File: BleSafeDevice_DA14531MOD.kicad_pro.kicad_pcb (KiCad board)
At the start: 2 copper layers, 43.5 x 33.5 mm, 19 parts, among them J1 SWD_DEBUG_PADS, J2 CURRENT_MEAS_PADS, SW1 PTS526SK15SMTR2 LFS, U4 DA14531MOD-00F01002

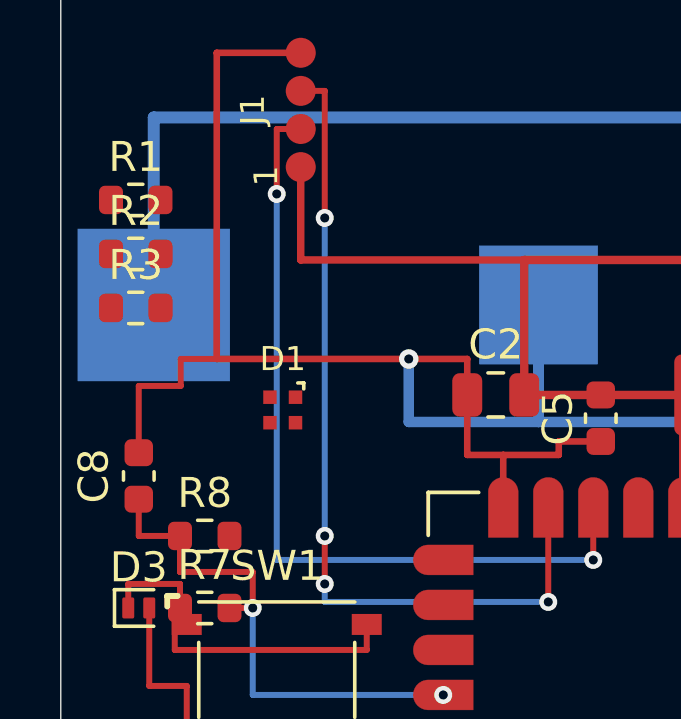
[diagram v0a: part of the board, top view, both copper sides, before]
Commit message: Route button pull-up and partial RGB LED nets
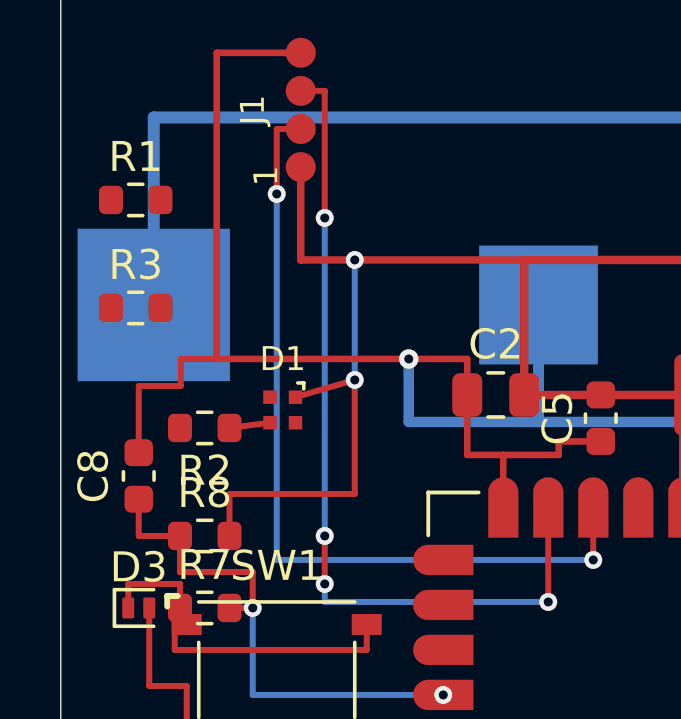
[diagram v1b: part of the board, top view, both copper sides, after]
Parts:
- moved R2 6.24 mm to (103.8, 112.6), turned to 180 degrees
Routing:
- net VCC: track 82.8 -> 100.1 mm, vias 0 -> 2
- net Net-(D1-GK): track 0.00 -> 1.36 mm
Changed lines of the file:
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@@
 	(footprint "Resistor_SMD:R_0603_1608Metric"
 		(layer "F.Cu")
-		(at 101.5 106.8)
+		(at 103.8 112.6 180)
 		(descr "Resistor SMD 0603 (1608 Metric), square (rectangular) end terminal, IPC-7351 nominal, (Body size source: IPC-SM-782 page 72, https://www.pcb-3d.com/wordpress/wp-content/uploads/ipc-sm-782a_amendment_1_and_2.pdf), generated with kicad-footprint-generator")
 		(tags "resistor")
 		(property "Reference" "R2"
-			(at 0 -1.43 0)
+			(at 0 -1.43 180)
 			(layer "F.SilkS")
 			(effects
@@
 		)
 		(property "Value" "1k"
-			(at 0 1.43 0)
+			(at 0 1.43 180)
 			(layer "F.Fab")
 			(effects
@@
 		)
 		(property "Datasheet" "~"
-			(at 0 0 0)
+			(at 0 0 180)
 			(layer "F.Fab")
 			(hide yes)
@@
 		)
 		(property "Description" "Resistor"
-			(at 0 0 0)
+			(at 0 0 180)
 			(layer "F.Fab")
 			(hide yes)
@@
 		(attr smd)
 		(fp_line
-			(start -0.237258 -0.5225)
-			(end 0.237258 -0.5225)
+			(start -0.237258 0.5225)
+			(end 0.237258 0.5225)
 			(stroke
 				(width 0.12)
@@
 		)
 		(fp_line
-			(start -0.237258 0.5225)
-			(end 0.237258 0.5225)
+			(start -0.237258 -0.5225)
+			(end 0.237258 -0.5225)
 			(stroke
 				(width 0.12)
@@
 		)
 		(fp_line
-			(start -1.48 -0.73)
-			(end 1.48 -0.73)
+			(start 1.48 0.73)
+			(end -1.48 0.73)
 			(stroke
 				(width 0.05)
@@
 		)
 		(fp_line
-			(start -1.48 0.73)
-			(end -1.48 -0.73)
+			(start 1.48 -0.73)
+			(end 1.48 0.73)
 			(stroke
 				(width 0.05)
@@
 		)
 		(fp_line
-			(start 1.48 -0.73)
-			(end 1.48 0.73)
+			(start -1.48 0.73)
+			(end -1.48 -0.73)
 			(stroke
 				(width 0.05)
@@
 		)
 		(fp_line
-			(start 1.48 0.73)
-			(end -1.48 0.73)
+			(start -1.48 -0.73)
+			(end 1.48 -0.73)
 			(stroke
 				(width 0.05)
@@
 		)
 		(fp_line
-			(start -0.8 -0.4125)
-			(end 0.8 -0.4125)
+			(start 0.8 0.4125)
+			(end -0.8 0.4125)
 			(stroke
 				(width 0.1)
@@
 		)
 		(fp_line
-			(start -0.8 0.4125)
-			(end -0.8 -0.4125)
+			(start 0.8 -0.4125)
+			(end 0.8 0.4125)
 			(stroke
 				(width 0.1)
@@
 		)
 		(fp_line
-			(start 0.8 -0.4125)
-			(end 0.8 0.4125)
+			(start -0.8 0.4125)
+			(end -0.8 -0.4125)
 			(stroke
 				(width 0.1)
@@
 		)
 		(fp_line
-			(start 0.8 0.4125)
-			(end -0.8 0.4125)
+			(start -0.8 -0.4125)
+			(end 0.8 -0.4125)
 			(stroke
 				(width 0.1)
@@
 		)
 		(fp_text user "${REFERENCE}"
-			(at 0 0 0)
+			(at 0 0 180)
 			(layer "F.Fab")
 			(effects
@@
 		)
 		(pad "1" smd roundrect
-			(at -0.825 0)
+			(at -0.825 0 180)
 			(size 0.8 0.95)
 			(layers "F.Cu" "F.Mask" "F.Paste")
@@
 		)
 		(pad "2" smd roundrect
-			(at 0.825 0)
+			(at 0.825 0 180)
 			(size 0.8 0.95)
 			(layers "F.Cu" "F.Mask" "F.Paste")
@@
 	)
 	(segment
+		(start 104.625 116.2)
+		(end 104.625 114.8)
+		(width 0.2)
+		(layer "F.Cu")
+		(net 3)
+	)
+	(segment
 		(start 139.2 121.4)
 		(end 139.2 107)
@@
 	)
 	(segment
+		(start 108.8 111)
+		(end 106.825 111.575)
+		(width 0.2)
+		(layer "F.Cu")
+		(net 3)
+	)
+	(segment
 		(start 117 111.5)
 		(end 120.025 111.5)
@@
 	)
 	(segment
+		(start 108.8 114.8)
+		(end 108.8 111)
+		(width 0.2)
+		(layer "F.Cu")
+		(net 3)
+	)
+	(segment
 		(start 139.2 107)
 		(end 114.45 107)
@@
 	)
 	(segment
+		(start 107 107)
+		(end 108.8 107)
+		(width 0.2)
+		(layer "F.Cu")
+		(net 3)
+	)
+	(segment
 		(start 131 107)
 		(end 131 109.925)
@@
 	)
 	(segment
+		(start 104.625 114.8)
+		(end 108.8 114.8)
+		(width 0.2)
+		(layer "F.Cu")
+		(net 3)
+	)
+	(segment
 		(start 139.2 107)
 		(end 131 107)
@@
 		(net 3)
 	)
+	(via
+		(at 108.8 107)
+		(size 0.6)
+		(drill 0.3)
+		(layers "F.Cu" "B.Cu")
+		(net 3)
+	)
+	(via
+		(at 108.8 111)
+		(size 0.6)
+		(drill 0.3)
+		(layers "F.Cu" "B.Cu")
+		(net 3)
+	)
+	(segment
+		(start 108.8 107)
+		(end 108.8 111)
+		(width 0.2)
+		(layer "B.Cu")
+		(net 3)
+	)
 	(segment
 		(start 102.975 116.2)
@@
 	)
 	(segment
+		(start 105.975 112.425)
+		(end 104.625 112.6)
+		(width 0.2)
+		(layer "F.Cu")
+		(net 6)
+	)
+	(segment

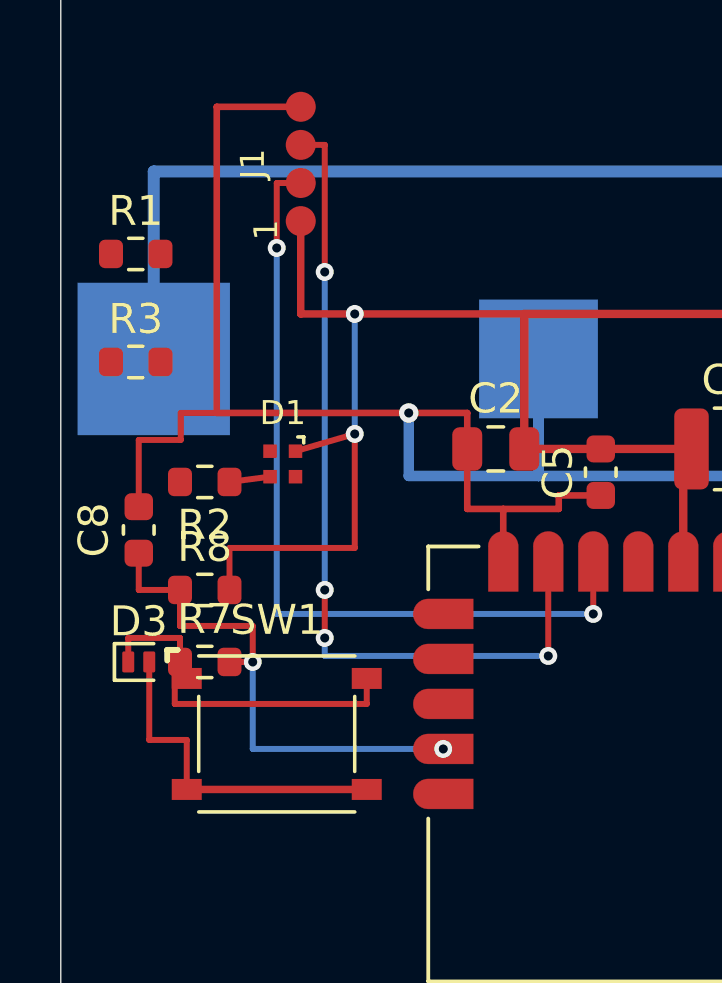
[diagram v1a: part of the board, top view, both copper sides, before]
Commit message: Simplify LED to red status channel and complete routing
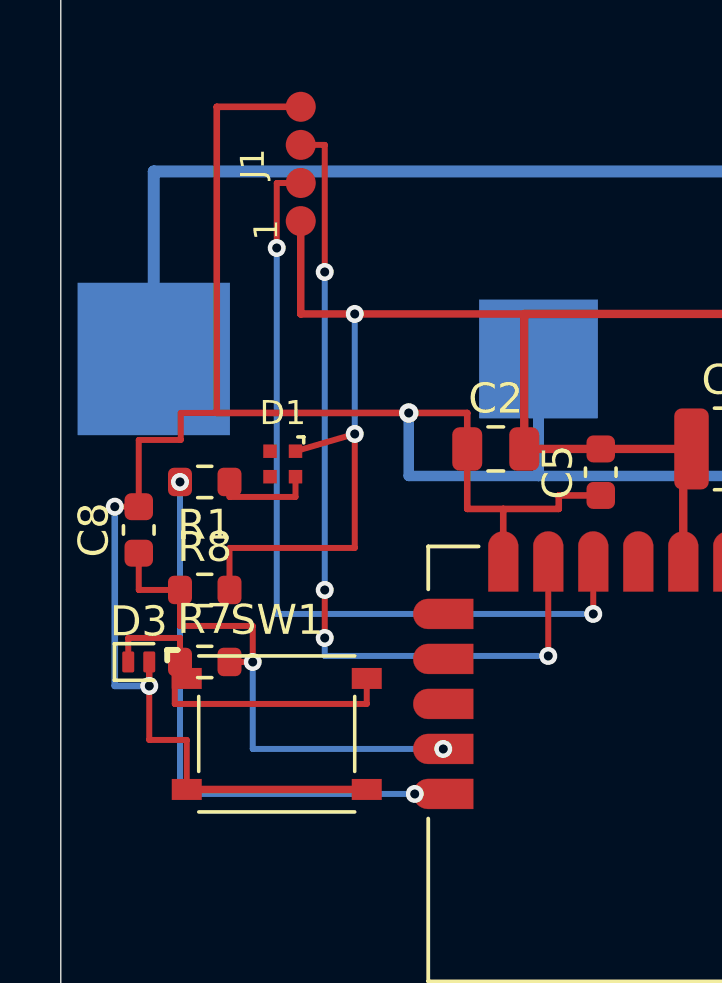
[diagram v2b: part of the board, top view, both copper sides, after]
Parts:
- removed R2, R3: 1k, Resistor_SMD:R_0603_1608Metric
- moved R1 7.94 mm to (103.8, 112.6), turned to 180 degrees
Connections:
- D1 pad 3: Net-(D1-GK) -> (no net)
- D1 pad 4: Net-(D1-BK) -> (no net)
- U4 pad J13: LED_G -> (no net)
- U4 pad J5: LED_B -> (no net)
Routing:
- net LED_R: track 0.00 -> 19.2 mm, vias 0 -> 2
- net GND: track 136.1 -> 144.8 mm, vias 3 -> 5
- net Net-(D1-RK): track 0.00 -> 3.38 mm
- net Net-(D1-GK): track 1.36 -> 0.00 mm
